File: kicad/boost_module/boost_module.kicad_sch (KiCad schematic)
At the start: 30 parts, among them J1 Conn_01x02, J2 Conn_01x02, J3 Conn_01x02, U1 OPA188xxDBV

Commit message: component selection
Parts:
- added C6: 2u2, capacitors:C_0603_1608Metric, symbol capacitors:C-2u2-50V-X5R-0603
- C1, C2, C4, C5: footprint Capacitor_SMD:C_0603_1608Metric_Pad1.08x0.95mm_HandSolder -> capacitors:C_0603_1608Metric; symbol Device:C -> capacitors:C-0u1-50V-X7R-0603; Dielectric (none) -> X7R; MPN1 (none) -> CL10B104KB8NNWC; Tolerance (none) -> 10%; Voltage (none) -> 50V
- C10: footprint Capacitor_SMD:C_0603_1608Metric_Pad1.08x0.95mm_HandSolder -> capacitors:C_1206_3216Metric; symbol Device:C -> capacitors:C-10u-25V-X7R-1206; Dielectric (none) -> X7R; MPN1 (none) -> CL31B106KAHNNNE; Tolerance (none) -> 10%; Voltage (none) -> 25V
- C14, C15: value 22U -> 22u; footprint Capacitor_SMD:C_1210_3225Metric_Pad1.33x2.70mm_HandSolder -> capacitors:C_1206_3216Metric; symbol Device:C -> capacitors:C-22u-10V-X7R-1206; Dielectric (none) -> X7R; MPN1 (none) -> CL31B226MPHNNNE; Tolerance (none) -> 20%; Voltage (none) -> 10V
- C3: value 10u -> 2u2; footprint Capacitor_SMD:C_0603_1608Metric_Pad1.08x0.95mm_HandSolder -> capacitors:C_0603_1608Metric; symbol Device:C -> capacitors:C-2u2-50V-X5R-0603; Dielectric (none) -> X5R; MPN1 (none) -> UMK107BBJ225KA-T; Tolerance (none) -> 10%; Voltage (none) -> 50V
- C7: footprint Capacitor_SMD:C_0603_1608Metric_Pad1.08x0.95mm_HandSolder -> capacitors:C_1206_3216Metric; symbol Device:C -> capacitors:C-0u1-50V-C0G/NP0-1206; Dielectric (none) -> CG0/NP0; MPN1 (none) -> CGA5L2C0G1H104J160AA; Tolerance (none) -> 5%; Voltage (none) -> 50V
- C8, C9: footprint Capacitor_SMD:C_0603_1608Metric_Pad1.08x0.95mm_HandSolder -> capacitors:C_0603_1608Metric; symbol Device:C -> capacitors:C-100p-50V-C0G/NP0-0603; Dielectric (none) -> C0G/NP0; MPN1 (none) -> CC0603JRNPO9BN101; Tolerance (none) -> 5%; Voltage (none) -> 50V
- D1, D3, D4: value D_TVS -> 12V 1A; footprint Diode_SMD:D_0603_1608Metric_Pad1.05x0.95mm_HandSolder -> SOD:D_SOD-323; symbol Device:D_TVS -> diodes:D_TVS_12V_1A; MPN1 (none) -> PJGBLC12C_R1_00001
- D2: value D -> 40V 500mA; footprint Diode_SMD:D_0603_1608Metric_Pad1.05x0.95mm_HandSolder -> SOD:D_SOD-323; symbol Device:D -> diodes:D_40V_500mA_SOD323; MPN1 (none) -> CMDSH05-4 TR PBFREE
- U1: value OPA188xxDBV -> OPA1677; footprint Package_TO_SOT_SMD:TSOT-23-5 -> SOT:TSOT-23-5; symbol Amplifier_Operational:OPA188xxDBV -> op_amps:OPA1677; MPN1 (none) -> OPA1677DBVR
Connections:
- net GND: now also C6.2
- net VCC: now also C6.1
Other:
- moved on the sheet: C1, C14, C15, C2, C3, C4, C8, C9, D1, D2, D3, J1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

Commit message: added 1590G2 enclosure footprint
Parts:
- added N1: 1590G2, hammond:1590G, symbol enclosures:1590G
- RV1: footprint Potentiometer_THT:Potentiometer_Bourns_3299W_Vertical -> potentiometers:Pot_RD901F-40-00D_Single_Vertical; symbol Device:R_Potentiometer -> resistors:RV_RD901F-40-15R1-B10K-00DL1; Power (none) -> xx mW; Tolerance (none) -> xx%
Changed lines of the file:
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@@
+    )
+  )
+  (symbol (lib_id "enclosures:1590G") (at 241.3 35.56 0) (unit 1)
+    (in_bom yes) (on_board yes) (dnp no) (fields_autoplaced)
+    (property "Reference" "N1" (at 245.11 35.2425 0)
+      (effects (font (size 1.27 1.27)) (justify left))
+    )
+    (property "Value" "1590G2" (at 245.11 37.7825 0)
+      (effects (font (size 1.27 1.27)) (justify left))
+    )
+    (property "Footprint" "hammond:1590G" (at 242.57 34.29 0)
+      (effects (font (size 1.27 1.27)) hide)
+    )
+    (property "Datasheet" "~" (at 242.57 34.29 0)
+      (effects (font (size 1.27 1.27)) hide)
+    )
+    (instances
+      (project "boost_module"
+        (path "/e54bd1be-7756-46cb-8e99-5674f5ef226a"
+          (reference "N1") (unit 1)
+        )
+      )
     )
   )
@@
     )
   )
-  (symbol (lib_id "Device:R_Potentiometer") (at 125.73 109.22 0) (mirror y) (unit 1)
+  (symbol (lib_id "resistors:RV_RD901F-40-15R1-B10K-00DL1") (at 125.73 109.22 0) (mirror y) (unit 1)
     (in_bom yes) (on_board yes) (dnp no)
     (property "Reference" "RV1" (at 128.27 109.855 0)
@@
       (effects (font (size 1.27 1.27)) (justify right))
     )
-    (property "Footprint" "Potentiometer_THT:Potentiometer_Bourns_3299W_Vertical" (at 125.73 109.22 0)
+    (property "Footprint" "potentiometers:Pot_RD901F-40-00D_Single_Vertical" (at 125.73 109.22 0)
       (effects (font (size 1.27 1.27)) hide)
     )
@@
       (effects (font (size 1.27 1.27)) hide)
     )
+    (property "Power" "xx mW" (at 125.73 109.22 0)
+      (effects (font (size 1.27 1.27)) hide)
+    )
+    (property "Tolerance" "xx%" (at 125.73 109.22 0)
+      (effects (font (size 1.27 1.27)) hide)
+    )
+    (property "MPN1" "" (at 125.73 109.22 0)
+      (effects (font (size 1.27 1.27)) hide)
+    )

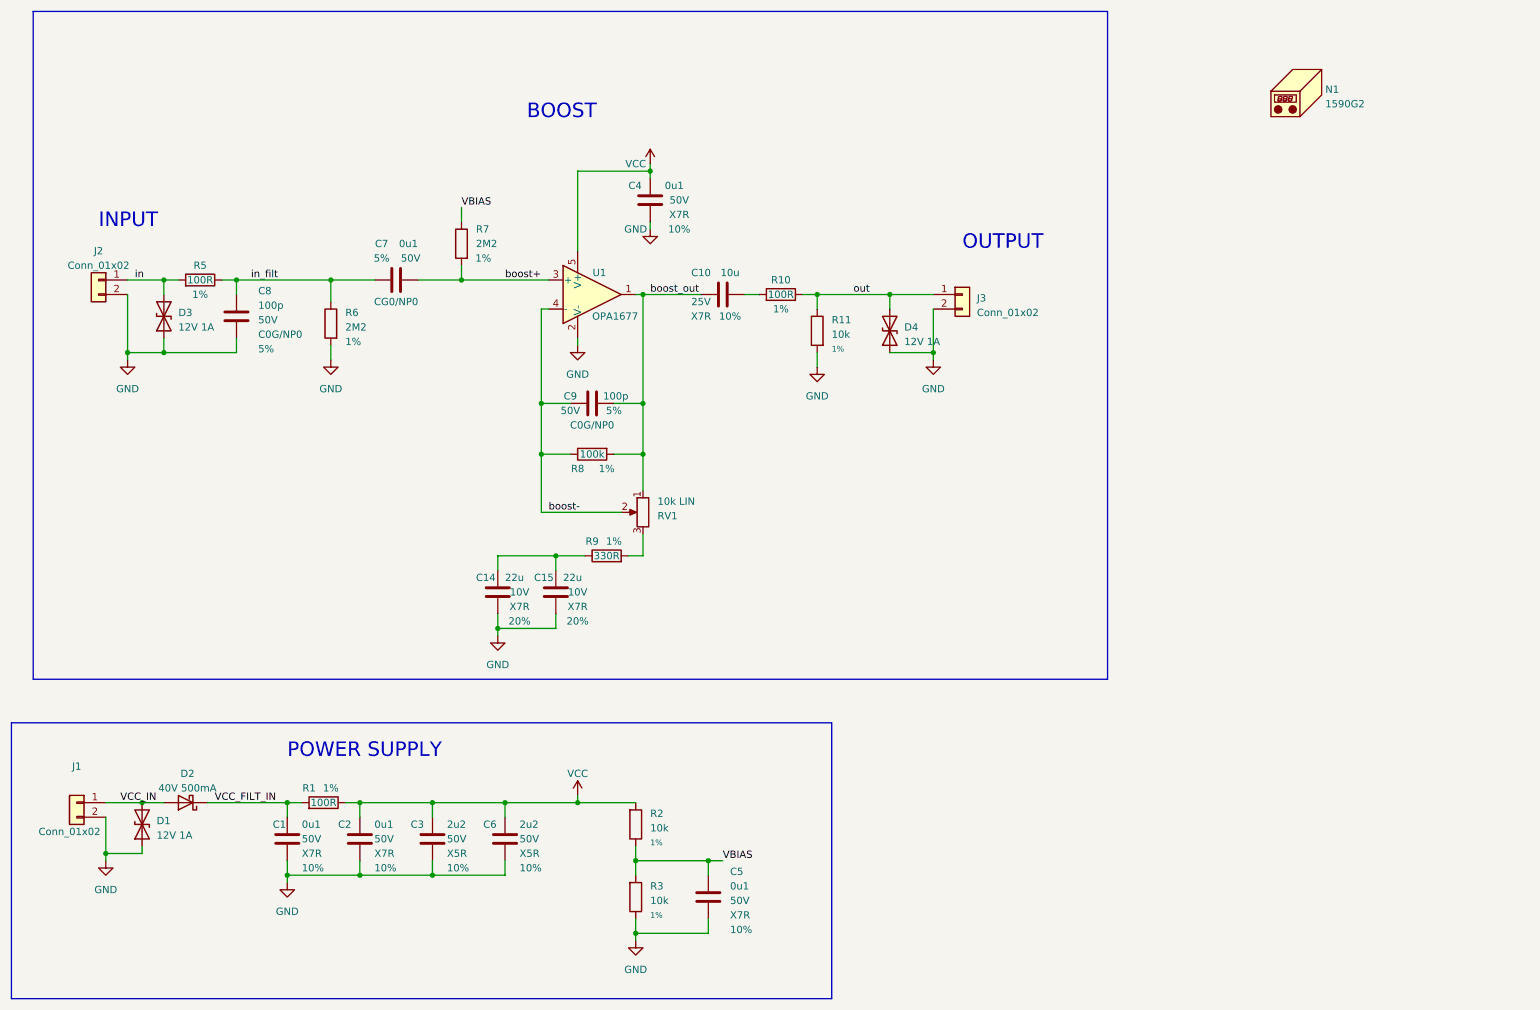
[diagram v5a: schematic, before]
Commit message: changed layout for 1591XXLTBU enclosure
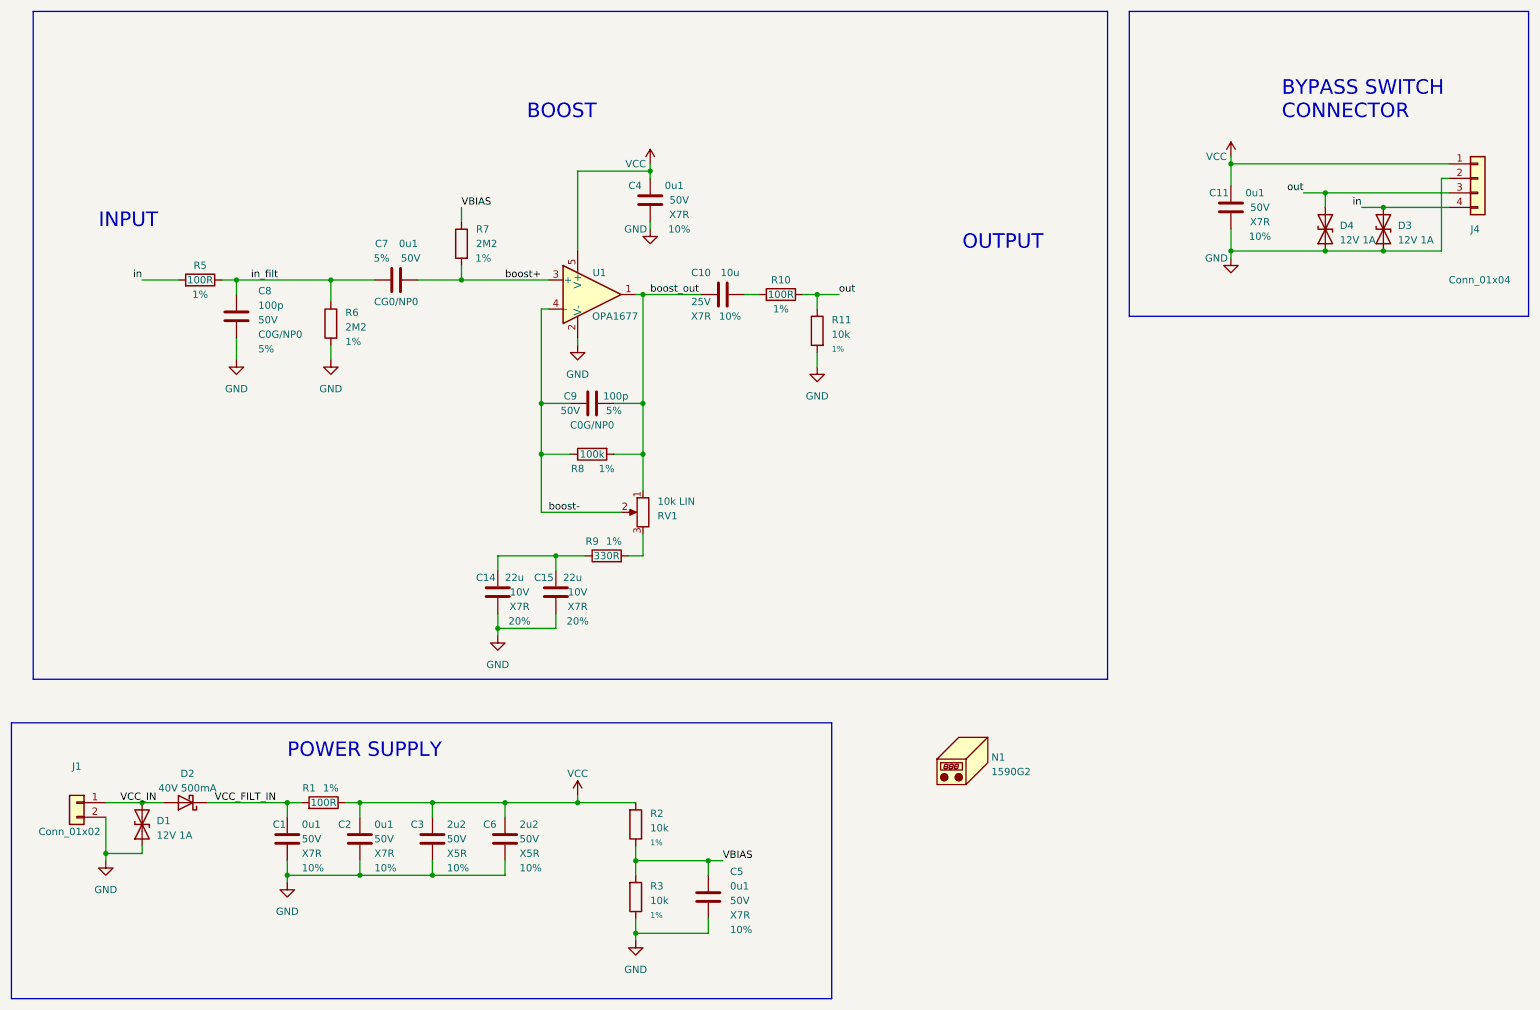
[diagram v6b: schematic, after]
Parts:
- removed J2, J3: Conn_01x02, Connector_PinHeader_2.54mm:PinHeader_1x02_P2.54mm_Vertical, symbol Connector_Generic:Conn_01x02
- added C11: 0u1, capacitors:C_0603_1608Metric, symbol capacitors:C-0u1-50V-X7R-0603
- added J4: Conn_01x04, connectors_headers:PinSocket_1x04_P2.54mm_Vertical, symbol connectors_headers:Conn_01x04_sckt_100mil_machine_pin
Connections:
- net GND: now also C11.2, J4.2 (Pin_2)
- net VCC: now also C11.1, J4.1 (Pin_1)
- net in: now also J4.4 (Pin_4)
- net out: now also J4.3 (Pin_3)
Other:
- note added: "BYPASS SWITCH CONNECTOR"
- moved on the sheet: D3, D4, N1

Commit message: placement and routing
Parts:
- added TP1, TP2, TP3, TP4, TP5: TestPoint, TestPoint:TestPoint_Pad_D1.0mm, symbol Connector:TestPoint
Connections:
- net GND: now also TP2.1
- net VBIAS: now also TP3.1
- net VCC: now also TP1.1
- net boost+: now also TP4.1
- net boost_out: now also TP5.1
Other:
- moved on the sheet: C10, C7, C8, R10, R11, R5, R6, R7
